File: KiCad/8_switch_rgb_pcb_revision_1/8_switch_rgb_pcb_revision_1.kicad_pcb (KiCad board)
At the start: 2 copper layers, 100 x 100 mm, 95 parts, among them SW0 SW0, SW1 SW1, SW2 SW2, SW3 SW3, SW4 SW4, SW5 SW5, SW6 SW6, SW7 SW7, U2 74HC165, Y1 16MHz

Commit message: Added pad for serial incase SPI fails.
Will move the ICs closer together to shorten the serial and clock lines.
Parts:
- added ?: , , F.Cu at (160.4, 122.6)
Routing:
- net Net-(U_Drain1-SER_OUT): track 0.00 -> 29.3 mm
- net GND: track 94.5 -> 109.5 mm
- net +5V: track 103.3 -> 117.2 mm
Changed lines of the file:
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@@
         (effects (font (size 1 1) (thickness 0.15)))
     )
-    (fp_text user "${REFERENCE}" (at 3.81 8.89) (layer "F.Fab")
+    (fp_text user "${REFERENCE}" (at 3.81 8.89 90) (layer "F.Fab")
         (effects (font (size 1 1) (thickness 0.15)))
     )
@@
         (effects (font (size 1 1) (thickness 0.15)))
     )
-    (fp_text user "${REFERENCE}" (at 3.81 16.51 90) (layer "F.Fab")
+    (fp_text user "${REFERENCE}" (at 3.81 16.51 -180) (layer "F.Fab")
         (effects (font (size 1 1) (thickness 0.15)))
     )
@@
     )
   )
+  (footprint "" (layer "F.Cu")
+    (at 160.44 122.59)
+    (fp_text reference "" (at 0 0) (layer "F.SilkS")
+        (effects (font (size 1.27 1.27) (thickness 0.15)))
+    )
+    (fp_text value "" (at 0 0) (layer "F.SilkS")
+        (effects (font (size 1.27 1.27) (thickness 0.15)))
+    )
+    (pad "14" thru_hole oval (at 0 0) (size 1.6 1.6) (drill 0.8) (layers "*.Cu" "*.Mask")
+      (net 80 "Net-(U_Drain1-SER_OUT)") (pinfunction "SER") (pintype "input"))
+  )
   (footprint "Package_DIP:DIP-16_W7.62mm_Socket" (layer "F.Cu")
     (at 133.62 117.93)
@@
         (effects (font (size 1 1) (thickness 0.15)))
     )
-    (fp_text user "${REFERENCE}" (at 3.81 8.89) (layer "F.Fab")
+    (fp_text user "${REFERENCE}" (at 3.81 8.89 90) (layer "F.Fab")
         (effects (font (size 1 1) (thickness 0.15)))
     )
@@
   (gr_circle (center 113.48 146.4) (end 114.48 146.4)
     (stroke (width 0.1) (type default)) (fill none) (layer "Edge.Cuts"))
+  (segment (start 133.51 143) (end 133.62 142.89) (width 2) (layer "F.Cu") (net 1))
   (segment (start 116.18 126.9) (end 119.18 129.9) (width 2) (layer "F.Cu") (net 1))
   (segment (start 149.88 143) (end 151.805 141.075) (width 2) (layer "F.Cu") (net 1))
   (segment (start 175.12 143) (end 195.12 143) (width 2) (layer "F.Cu") (net 1))
-  (segment (start 119.88 143) (end 149.88 143) (width 2) (layer "F.Cu") (net 1))
+  (segment (start 133.62 142.89) (end 133.62 135.71) (width 2) (layer "F.Cu") (net 1))
+  (segment (start 119.88 143) (end 133.51 143) (width 2) (layer "F.Cu") (net 1))
   (segment (start 119.18 131.6) (end 119.18 142.3) (width 2) (layer "F.Cu") (net 1))
+  (segment (start 133.51 143) (end 149.88 143) (width 2) (layer "F.Cu") (net 1))
   (segment (start 151.805 141.075) (end 163.195 141.075) (width 2) (layer "F.Cu") (net 1))
   (segment (start 119.18 129.9) (end 119.18 131.6) (width 2) (layer "F.Cu") (net 1))
@@
   (segment (start 119.18 142.3) (end 119.88 143) (width 2) (layer "F.Cu") (net 1))
   (segment (start 163.195 141.075) (end 165.12 143) (width 2) (layer "F.Cu") (net 1))
+  (segment (start 149.88 135.35) (end 149.82 135.29) (width 2) (layer "B.Cu") (net 1))
+  (segment (start 149.88 143) (end 149.88 135.35) (width 2) (layer "B.Cu") (net 1))
   (segment (start 119.88 148) (end 195.12 148) (width 2) (layer "F.Cu") (net 6))
+  (segment (start 130.82 117.93) (end 133.62 117.93) (width 2) (layer "B.Cu") (net 6))
   (segment (start 125.42 126.79) (end 125.42 144.71) (width 2) (layer "B.Cu") (net 6))
   (segment (start 122.18 126.9) (end 125.31 126.9) (width 2) (layer "B.Cu") (net 6))
+  (segment (start 125.42 126.79) (end 125.42 123.33) (width 2) (layer "B.Cu") (net 6))
   (segment (start 125.31 126.9) (end 125.42 126.79) (width 2) (layer "B.Cu") (net 6))
+  (segment (start 125.42 123.33) (end 130.82 117.93) (width 2) (layer "B.Cu") (net 6))
   (segment (start 125.42 144.71) (end 122.13 148) (width 2) (layer "B.Cu") (net 6))
   (segment (start 122.13 148) (end 119.88 148) (width 2) (layer "B.Cu") (net 6))
@@
   (segment (start 156.26 93.02) (end 157.239 93.999) (width 0.25) (layer "B.Cu") (net 13))
   (segment (start 149.96 74.02) (end 152.15 71.83) (width 0.25) (layer "B.Cu") (net 13))
+  (segment (start 150.060991 136.64) (end 142.17 136.64) (width 0.25) (layer "F.Cu") (net 80))
+  (segment (start 153.775 126.255) (end 153.775 132.925991) (width 0.25) (layer "F.Cu") (net 80))
+  (segment (start 153.775 132.925991) (end 150.060991 136.64) (width 0.25) (layer "F.Cu") (net 80))
+  (segment (start 142.17 136.64) (end 141.24 135.71) (width 0.25) (layer "F.Cu") (net 80))
+  (segment (start 157.44 122.59) (end 160.44 122.59) (width 0.25) (layer "F.Cu") (net 80))
+  (segment (start 157.44 122.59) (end 153.775 126.255) (width 0.25) (layer "F.Cu") (net 80))
   (segment (start 147.42 58.78) (end 148.399 59.759) (width 0.25) (layer "F.Cu") (net 87))
   (segment (start 148.399 59.759) (end 159.041 59.759) (width 0.25) (layer "F.Cu") (net 87))

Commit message: Placed the registers and MCU
I think it is doable orientation.
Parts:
- removed ?: , 
- added R40: 33Ω, Resistor_THT:R_Axial_DIN0204_L3.6mm_D1.6mm_P5.08mm_Horizontal, F.Cu at (-80.0, 146.2)
- added R41: 33Ω, Resistor_THT:R_Axial_DIN0204_L3.6mm_D1.6mm_P5.08mm_Horizontal, F.Cu at (-80.0, 149.4)
- added R42: 33Ω, Resistor_THT:R_Axial_DIN0204_L3.6mm_D1.6mm_P5.08mm_Horizontal, F.Cu at (-80.0, 152.5)
- added R43: 33Ω, Resistor_THT:R_Axial_DIN0204_L3.6mm_D1.6mm_P5.08mm_Horizontal, F.Cu at (-80.0, 155.7)
- added R44: 33Ω, Resistor_THT:R_Axial_DIN0204_L3.6mm_D1.6mm_P5.08mm_Horizontal, F.Cu at (-80.0, 158.8)
- added R45: 33Ω, Resistor_THT:R_Axial_DIN0204_L3.6mm_D1.6mm_P5.08mm_Horizontal, F.Cu at (157.5, 138.2)
- added R46: 33Ω, Resistor_THT:R_Axial_DIN0204_L3.6mm_D1.6mm_P5.08mm_Horizontal, F.Cu at (-80.0, 165.1)
- R39: footprint Resistor_THT:R_Axial_DIN0204_L3.6mm_D1.6mm_P2.54mm_Vertical -> Resistor_THT:R_Axial_DIN0204_L3.6mm_D1.6mm_P5.08mm_Horizontal
- moved R6 357.8 mm to (191.8, 86.2), turned to -90 degrees
- moved R11 354.3 mm to (200.8, 86.2), turned to -90 degrees
- moved R8 350.3 mm to (182.8, 86.2), turned to -90 degrees
- moved R10 327.0 mm to (173.8, 86.2), turned to -90 degrees
- moved R5 298.4 mm to (132.2, 86.2), turned to -90 degrees
- moved R12 295.9 mm to (141.2, 86.2), turned to -90 degrees
- moved R7 291.1 mm to (123.2, 86.2), turned to -90 degrees
- moved R9 267.4 mm to (114.2, 86.2), turned to -90 degrees
- moved R3 253.6 mm to (83.8, 66.2)
- moved R4 249.1 mm to (82.3, 83.6)
- moved R13 239.5 mm to (87.7, 115.5)
- moved R19 239.2 mm to (87.6, 122.5)
- moved R2 214.2 mm to (49.4, 89.5), turned to -90 degrees
- moved R21 204.5 mm to (52.1, 125.5)
- moved R1 203.7 mm to (40.6, 97.0), turned to 90 degrees
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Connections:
- MCU_1 pad 16: Net-(MCU_1-PB2) -> unconnected-(MCU_1-PB2-Pad16)
- MCU_1 pad 19: Net-(MCU_1-PB4) -> Net-(MCU_1-PB5)
- R22 pad 1: Net-(MCU_1-PB4) -> Net-(MCU_1-PB5)
- R36 pad 1: Net-(MCU_1-PB2) -> Net-(U_Drain1-SER_IN)
- R39 pad 1: Net-(MCU_1-PB1) -> Net-(U_Trans1-RCLK)
- R39 pad 2: Net-(MCU_1-PB0) -> Net-(U_Drain1-RCLK)
- U2 pad 1: Net-(MCU_1-PD7) -> Net-(U2-~{PL})
- U2 pad 2: Net-(MCU_1-PB4) -> Net-(MCU_1-PB5)
- U2 pad 9: Net-(MCU_1-PB3) -> Net-(U2-Q7)
- U_Drain1 pad 10: Net-(MCU_1-PB0) -> Net-(U_Drain1-RCLK)
- U_Drain1 pad 15: Net-(MCU_1-PB4) -> Net-(MCU_1-PB5)
- U_Drain1 pad 2: Net-(MCU_1-PB2) -> Net-(U_Drain1-SER_IN)
- U_Trans1 pad 11: Net-(MCU_1-PB4) -> Net-(MCU_1-PB5)
- U_Trans1 pad 12: Net-(MCU_1-PB1) -> Net-(U_Trans1-RCLK)
- U_Trans1 pad 14: Net-(U_Drain1-SER_OUT) -> Net-(U_Trans1-SER)
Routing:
- net GND: track 109.5 -> 367.9 mm
- net +5V: track 117.2 -> 278.2 mm
- net Net-(U_Drain1-SER_OUT): track 29.3 -> 2.48 mm

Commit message: Added all components to board. But the amount of terrible track management is impossible without sleep. I had hopped to be done today, but the remaining tracks and DRC-check will take 2 hours, 4-8 if i'm tired and keep shooting my own foot.
The important data and clock need to be keept in acute memory.
Data and clock includes OE and register-clocks.

I tracked them at the verry begining, so it should be fine.
Just need to be REALLY careful.
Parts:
- removed CU2: 100nF, Capacitor_THT:C_Disc_D5.0mm_W2.5mm_P5.00mm
- removed NC1, NC2, NC3, NC4: Screw Terminal, TerminalBlock_Phoenix:TerminalBlock_Phoenix_MPT-0,5-2-2.54_1x02_P2.54mm_Horizontal
- removed R16, R18: 0Ω, Resistor_THT:R_Axial_DIN0204_L3.6mm_D1.6mm_P2.54mm_Vertical
- added ?: , , F.Cu at (117.5, 113.8)
- added ?: , , F.Cu at (137.8, 113.8)
- added ?: , , F.Cu at (197.3, 104.7)
- added ?: , , F.Cu at (158.5, 133.1)
- added ?: , , F.Cu at (140.4, 113.8)
- added ?: , , F.Cu at (142.9, 113.8)
- added ?: , , F.Cu at (198.3, 117.8)
- added ?: , , F.Cu at (122.6, 113.8)
- added ?: , , F.Cu at (158.5, 135.6)
- added ?: , , F.Cu at (135.3, 113.8)
- moved T_HEX_1 349.2 mm to (200.8, 69.0), turned to -90 degrees
- moved T_HEX_0 339.1 mm to (191.8, 69.0), turned to -90 degrees
- moved T_DEC_2 329.1 mm to (182.8, 69.0), turned to -90 degrees
- moved PWR_Screw1 317.9 mm to (203.9, 100.7), turned to 90 degrees
- moved RGB2 317.5 mm to (203.9, 120.3), turned to 90 degrees
- moved Serial_Screw1 310.1 mm to (203.9, 113.8), turned to 90 degrees
- moved RGB1 310.0 mm to (203.9, 107.2), turned to 90 degrees
- moved R25 298.5 mm to (198.7, 133.1), turned to 90 degrees
- moved R26 296.8 mm to (192.3, 64.4)
- moved R35 292.4 mm to (176.3, 112.4), turned to 180 degrees
- moved R23 291.6 mm to (176.3, 118.0), turned to 90 degrees
- moved T_DEC_1 278.4 mm to (132.2, 69.0), turned to -90 degrees
- moved R22 278.1 mm to (178.4, 122.9), turned to 90 degrees
- moved R24 273.1 mm to (172.4, 140.0)
- moved R44 272.0 mm to (191.2, 138.8)
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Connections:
- MCU_1 pad 12: unconnected-(MCU_1-PD6-Pad12) -> Net-(MCU_1-PD6)
- MCU_1 pad 21: Net-(MCU_1-AREF) -> unconnected-(MCU_1-AREF-Pad21)
- MCU_1 pad 27: unconnected-(MCU_1-PC4-Pad27) -> Net-(MCU_1-PC4)
- MCU_1 pad 28: unconnected-(MCU_1-PC5-Pad28) -> Net-(MCU_1-PC5)
- R20 pad 1: unconnected-(R20-Pad1) -> Net-(RGB1-Pin_1)
- R24 pad 1: Net-(SW_Mem1-B) -> Net-(MCU_1-PD6)
- R25 pad 1: Net-(SW__WR1-B) -> Net-(MCU_1-PC4)
- R26 pad 1: Net-(SW_Serr1-B) -> Net-(MCU_1-PC5)
- RGB1 pad 1: unconnected-(RGB1-Pin_1-Pad1) -> Net-(RGB1-Pin_1)
- SW_Mem1 pad 2: Net-(SW_Mem1-B) -> Net-(MCU_1-PD6)
- SW_Serr1 pad 2: Net-(SW_Serr1-B) -> Net-(MCU_1-PC5)
- SW__WR1 pad 2: Net-(SW__WR1-B) -> Net-(MCU_1-PC4)
- U2 pad 10: unconnected-(U2-DS-Pad10) -> GND
- U_Trans1 pad 13: Net-(U_Trans1-~{OE}) -> Net-(MCU_1-PD2)
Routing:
- net +5V: track 278.2 -> 583.1 mm
- net Net-(D0-A): track 0.00 -> 174.1 mm
- net Net-(MCU_1-PB4): track 0.00 -> 136.7 mm, vias 0 -> 1
- net Net-(U_Drain1-DRAIN7): track 0.00 -> 119.3 mm, vias 0 -> 2
- net Net-(MCU_1-PD6): track 0.00 -> 113.8 mm
- net Net-(U_Drain1-DRAIN6): track 0.00 -> 111.6 mm, vias 0 -> 3
- net Net-(MCU_1-PC5): track 0.00 -> 111.2 mm, vias 0 -> 2
- net GND: track 367.9 -> 471.9 mm
- net Net-(T_HEX_1-E): track 0.00 -> 91.9 mm, vias 0 -> 2
- net Net-(T_HEX_0-E): track 0.00 -> 83.9 mm, vias 0 -> 2
- net Net-(U2-~{PL}): track 0.00 -> 81.7 mm, vias 0 -> 1
- net Net-(MCU_1-PC4): track 0.00 -> 77.5 mm, vias 0 -> 1
- net Net-(MCU_1-PD1): track 0.00 -> 70.5 mm, vias 0 -> 2
- net Net-(MCU_1-PB5): track 0.00 -> 68.5 mm
- net Net-(U_Drain1-RCLK): track 0.00 -> 66.3 mm
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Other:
- board text added: "+5V"
- board text added: "GND"
- board text added: "NC"
- board text added: "RGB1"
- board text added: "RGB2"
- board text added: "RX"
- board text added: "TX"
- board text added: "Term-5V"
- board text added: "Term-GND"

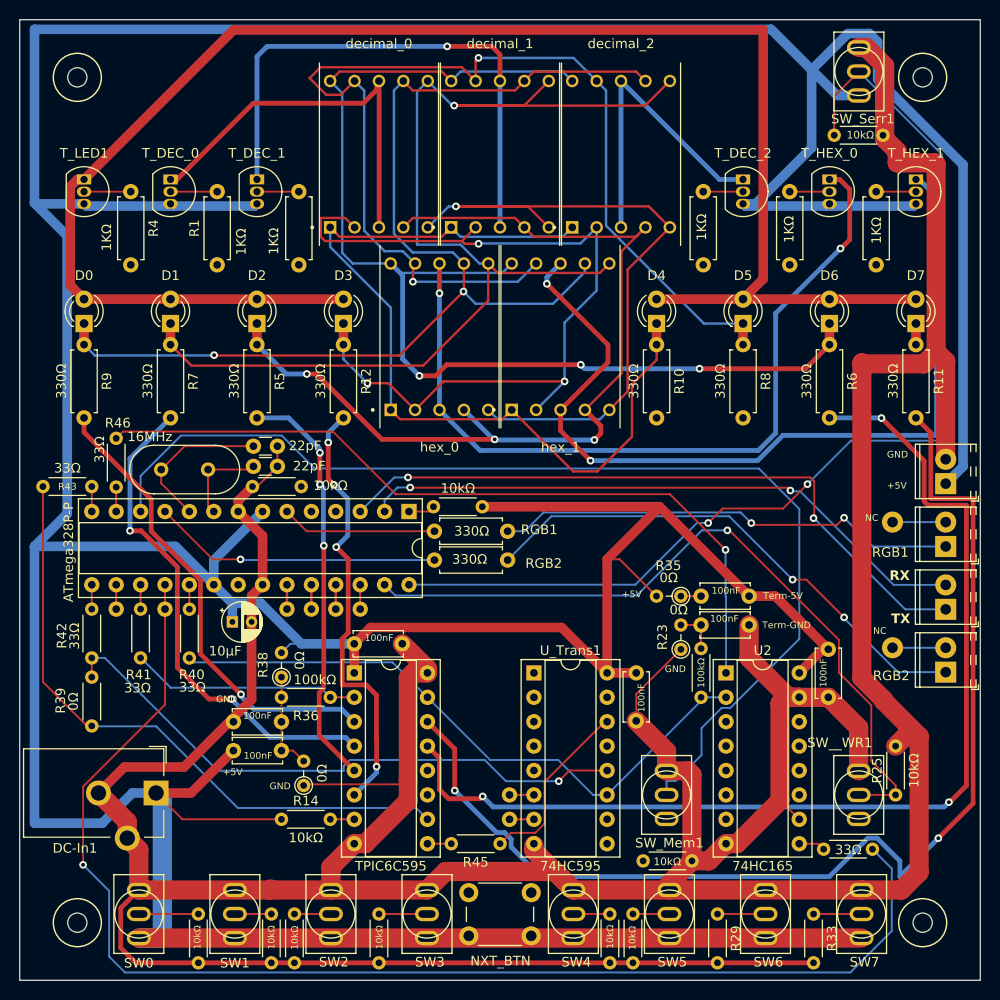
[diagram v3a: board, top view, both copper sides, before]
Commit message: Made GND 1 mm, aswell as 5v. Will Maybe fill the entire plane with GND at the end.
Depends how saddened the DRC will make me.
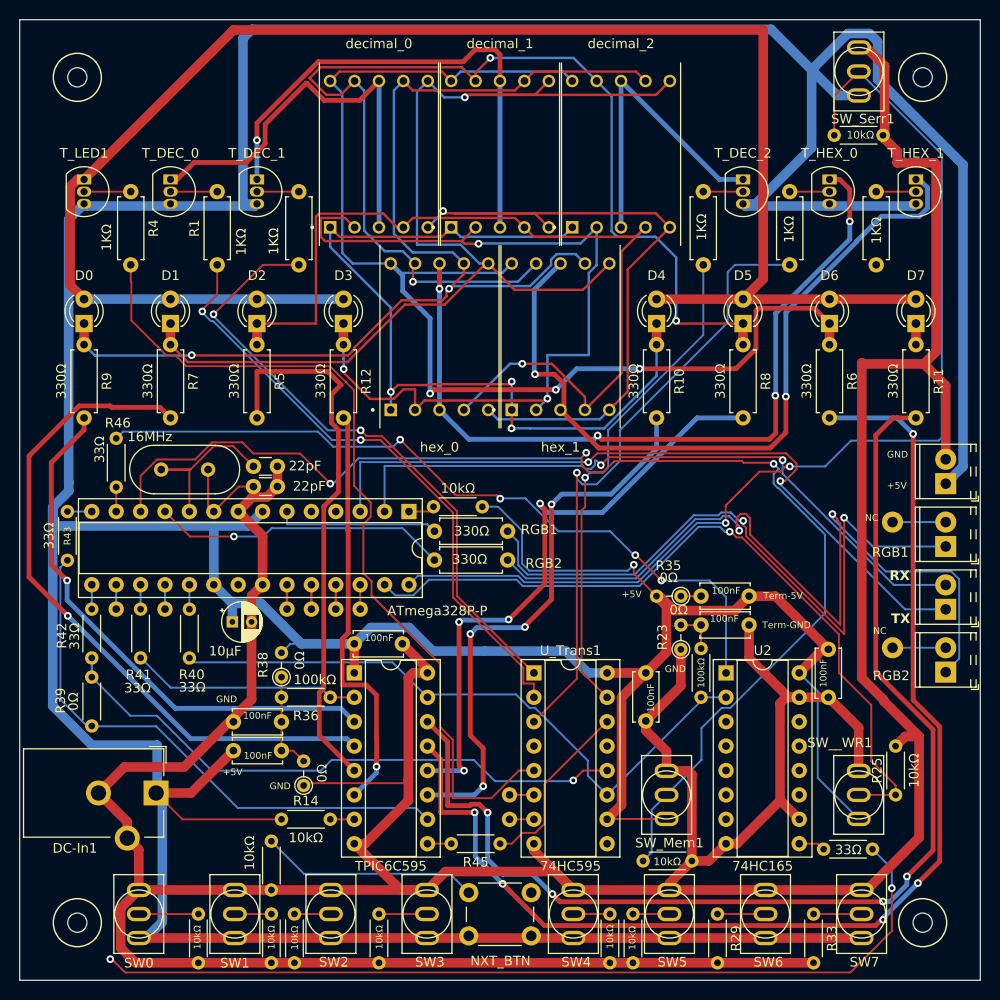
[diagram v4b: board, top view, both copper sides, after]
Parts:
- moved R15 37.1 mm to (133.7, 137.9), turned to -90 degrees
- moved R43 3.63 mm to (112.4, 103.6), turned to -90 degrees
- moved C2 2.10 mm to (131.8, 98.9)
- moved C1 2.10 mm to (134.3, 101.0)
- moved C_DRAIN0 1.00 mm to (172.7, 120.4)
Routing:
- net Net-(U_Trans1-QF): track 0.00 -> 89.1 mm
- net Net-(U_Trans1-QD): track 0.00 -> 65.3 mm, vias 0 -> 1
- net Net-(U_Trans1-QB): track 0.00 -> 65.1 mm, vias 0 -> 2
- net Net-(U_Drain1-DRAIN5): track 0.00 -> 64.4 mm, vias 0 -> 4
- net Net-(U_Trans1-QC): track 0.00 -> 64.0 mm, vias 0 -> 2
- net Net-(U_Drain1-DRAIN4): track 0.00 -> 59.4 mm, vias 0 -> 4
- net Net-(U_Trans1-QA): track 0.00 -> 52.1 mm, vias 0 -> 1
- net Net-(MCU_1-PB4): track 136.7 -> 95.6 mm, vias 1 -> 2
- net Net-(RGB2-Pin_1): track 54.3 -> 85.0 mm
- net Net-(MCU_1-PD3): track 0.00 -> 22.8 mm
- net Net-(RGB1-Pin_1): track 48.5 -> 70.9 mm
- net Net-(U_Drain1-DRAIN1): track 52.3 -> 71.2 mm, vias 2 -> 1
- net Net-(MCU_1-PD6): track 113.8 -> 129.4 mm, vias 0 -> 3
- net Net-(U_Drain1-DRAIN2): track 43.3 -> 57.4 mm, vias 3 -> 0
- net Net-(U_Drain1-DRAIN6): track 111.6 -> 124.9 mm, vias 3 -> 5
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
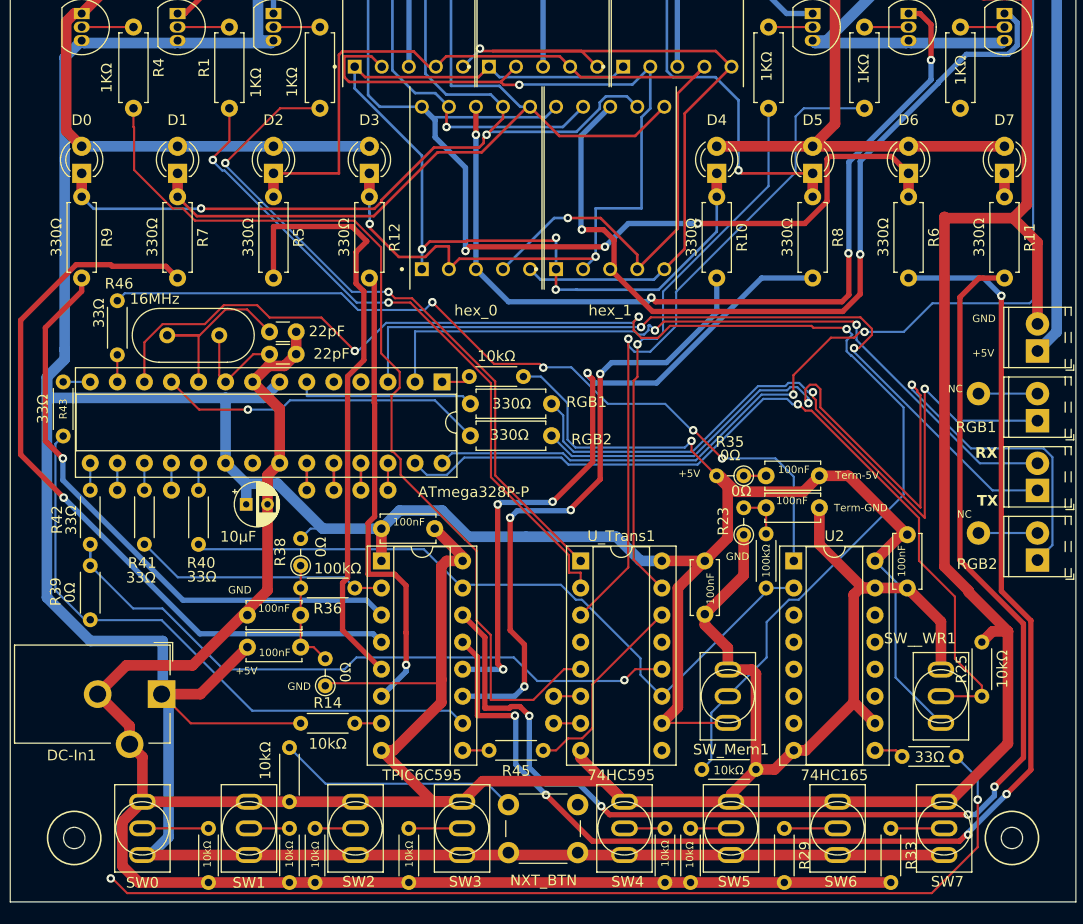
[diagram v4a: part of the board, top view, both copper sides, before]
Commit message: Connected all traces. Will now run DRC This is the last 2-layer board with more than 10 components I ever create.
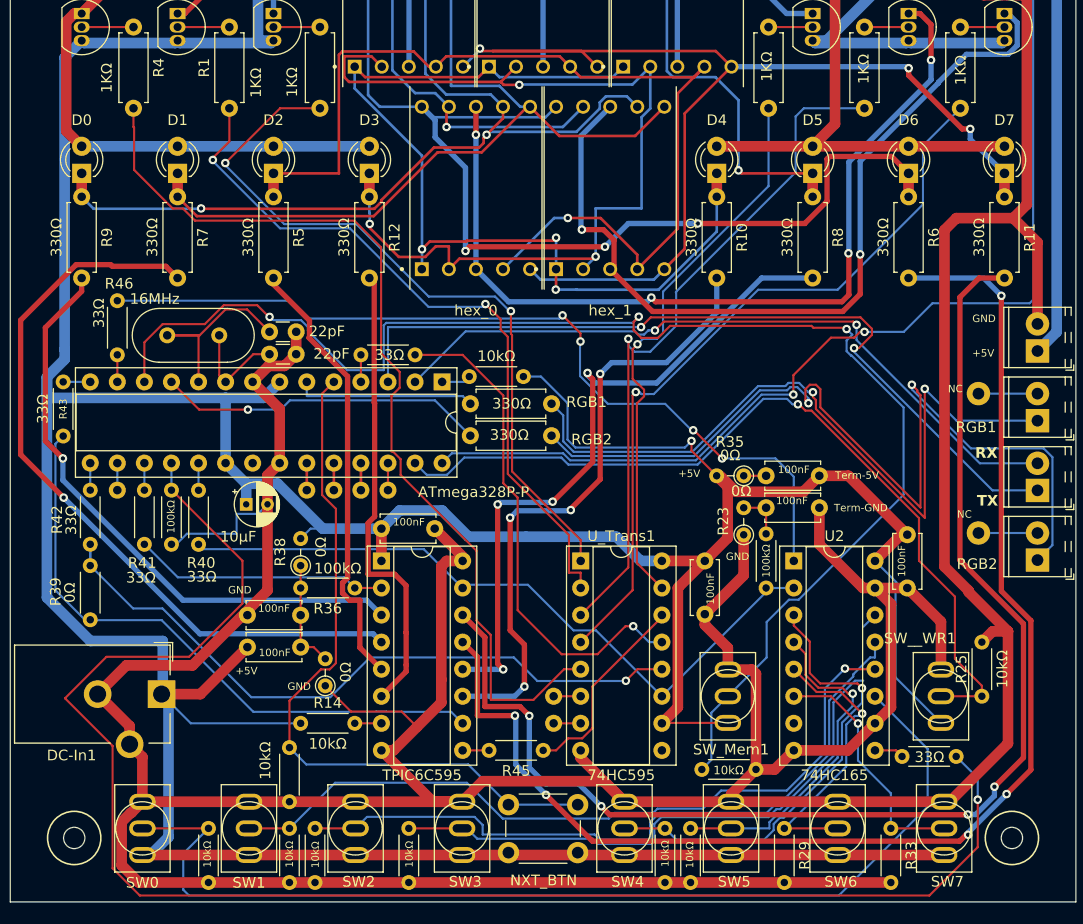
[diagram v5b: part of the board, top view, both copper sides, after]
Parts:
- removed the ? at (122.6, 113.8)
- added R16: 100kΩ, Resistor_THT:R_Axial_DIN0204_L3.6mm_D1.6mm_P5.08mm_Horizontal, F.Cu at (122.6, 113.8)
- added R18: 33Ω, Resistor_THT:R_Axial_DIN0204_L3.6mm_D1.6mm_P5.08mm_Horizontal, F.Cu at (140.4, 101.1)
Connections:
- U_Trans1 pad 13: Net-(MCU_1-PD2) -> Net-(U_Trans1-~{OE})
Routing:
- net Net-(SW0-B): track 6.20 -> 98.9 mm
- net Net-(U_Trans1-QE): track 0.00 -> 71.2 mm, vias 0 -> 1
- net Net-(SW1-B): track 3.80 -> 71.3 mm, vias 0 -> 1
- net Net-(SW2-B): track 3.80 -> 66.9 mm
- net Net-(MCU_1-PB4): track 95.6 -> 147.6 mm, vias 2 -> 1
- net Net-(SW3-B): track 5.00 -> 55.0 mm
- net Net-(U_Trans1-~{OE}): track 0.00 -> 47.5 mm, vias 0 -> 1
- net Net-(MCU_1-PD3): track 22.8 -> 66.9 mm
- net Net-(SW4-B): track 3.80 -> 43.3 mm, vias 0 -> 1
- net Net-(D7-K): track 74.3 -> 105.0 mm, vias 1 -> 3
- net Net-(SW5-B): track 3.80 -> 32.2 mm, vias 0 -> 1
- net Net-(SW6-B): track 5.00 -> 27.2 mm, vias 0 -> 1
- net Net-(SW7-B): track 5.00 -> 23.2 mm, vias 0 -> 1
- net Net-(U_Drain1-DRAIN2): track 57.4 -> 41.9 mm
- net GND: track 470.3 -> 480.8 mm
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
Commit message: Added 3d And moved dot marking the orintation of 7-seg to within footprint.
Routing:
- net Net-(SW3-B): track 55.0 -> 59.6 mm
- net Net-(D3-K): track 92.3 -> 89.7 mm
- net Net-(D1-K): track 117.0 -> 119.4 mm
- net Net-(D5-K): track 117.8 -> 116.4 mm
- net Net-(U_Trans1-QF): track 89.1 -> 90.3 mm
- net Net-(SW2-B): track 66.9 -> 67.8 mm, vias 0 -> 1
- net Net-(U_Trans1-QE): track 71.2 -> 70.5 mm
